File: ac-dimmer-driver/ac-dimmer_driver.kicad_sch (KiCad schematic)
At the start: 10 parts, among them J1 Conn_01x08_Pin, J2 Conn_01x08_Pin, U1 MCP4451

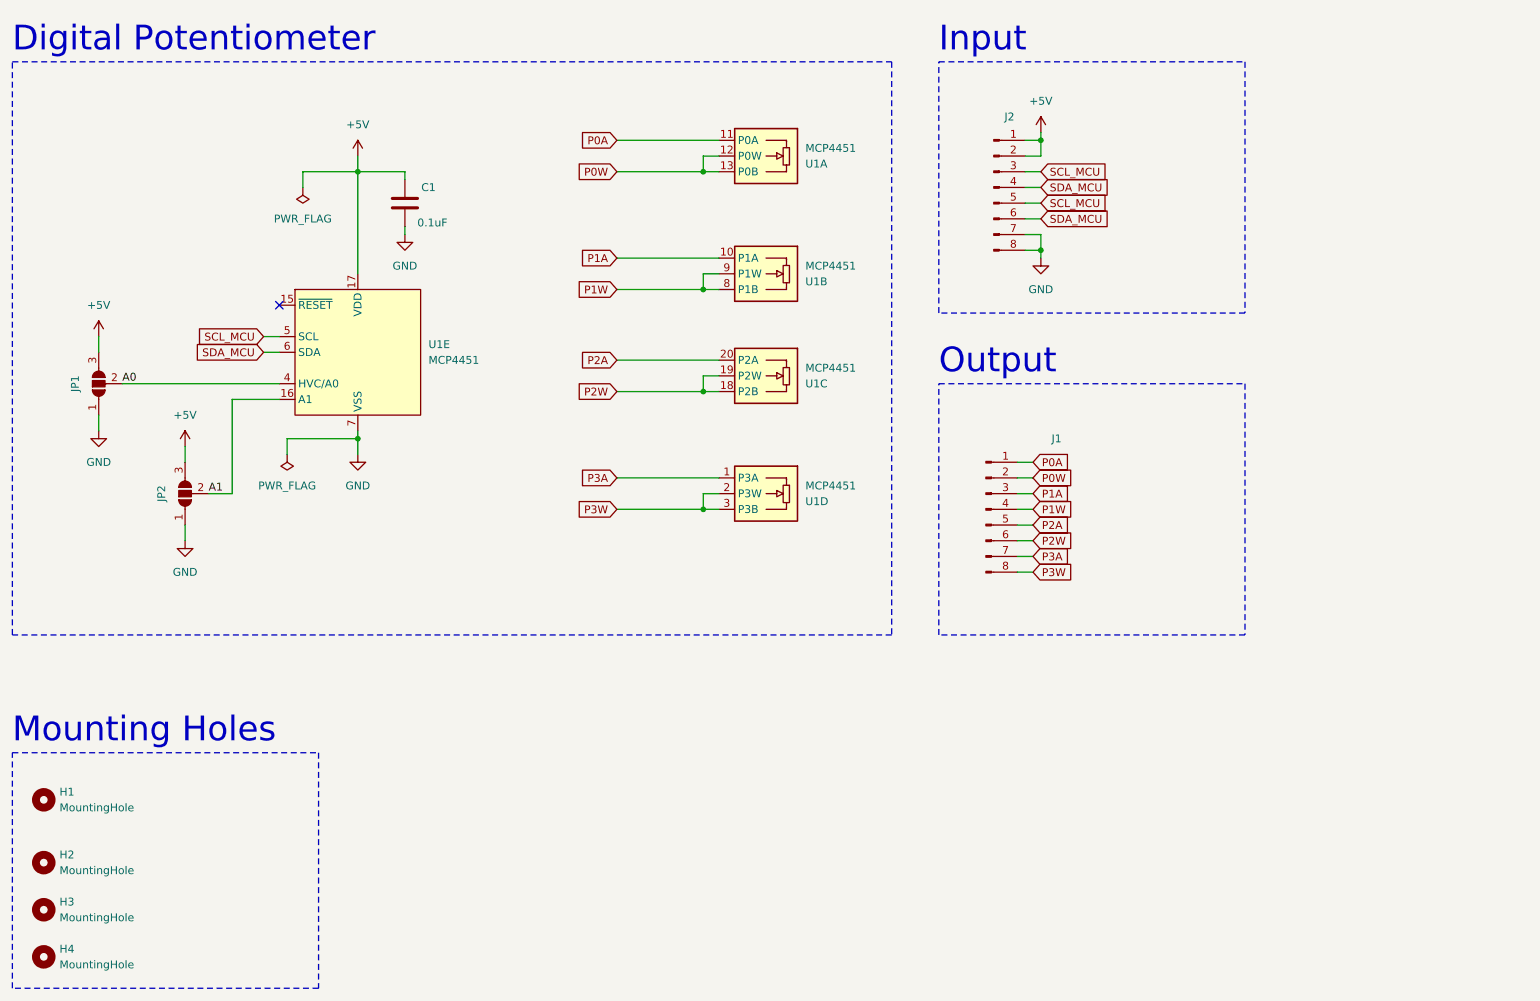
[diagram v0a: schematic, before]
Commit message: Create production files for ac dimmer
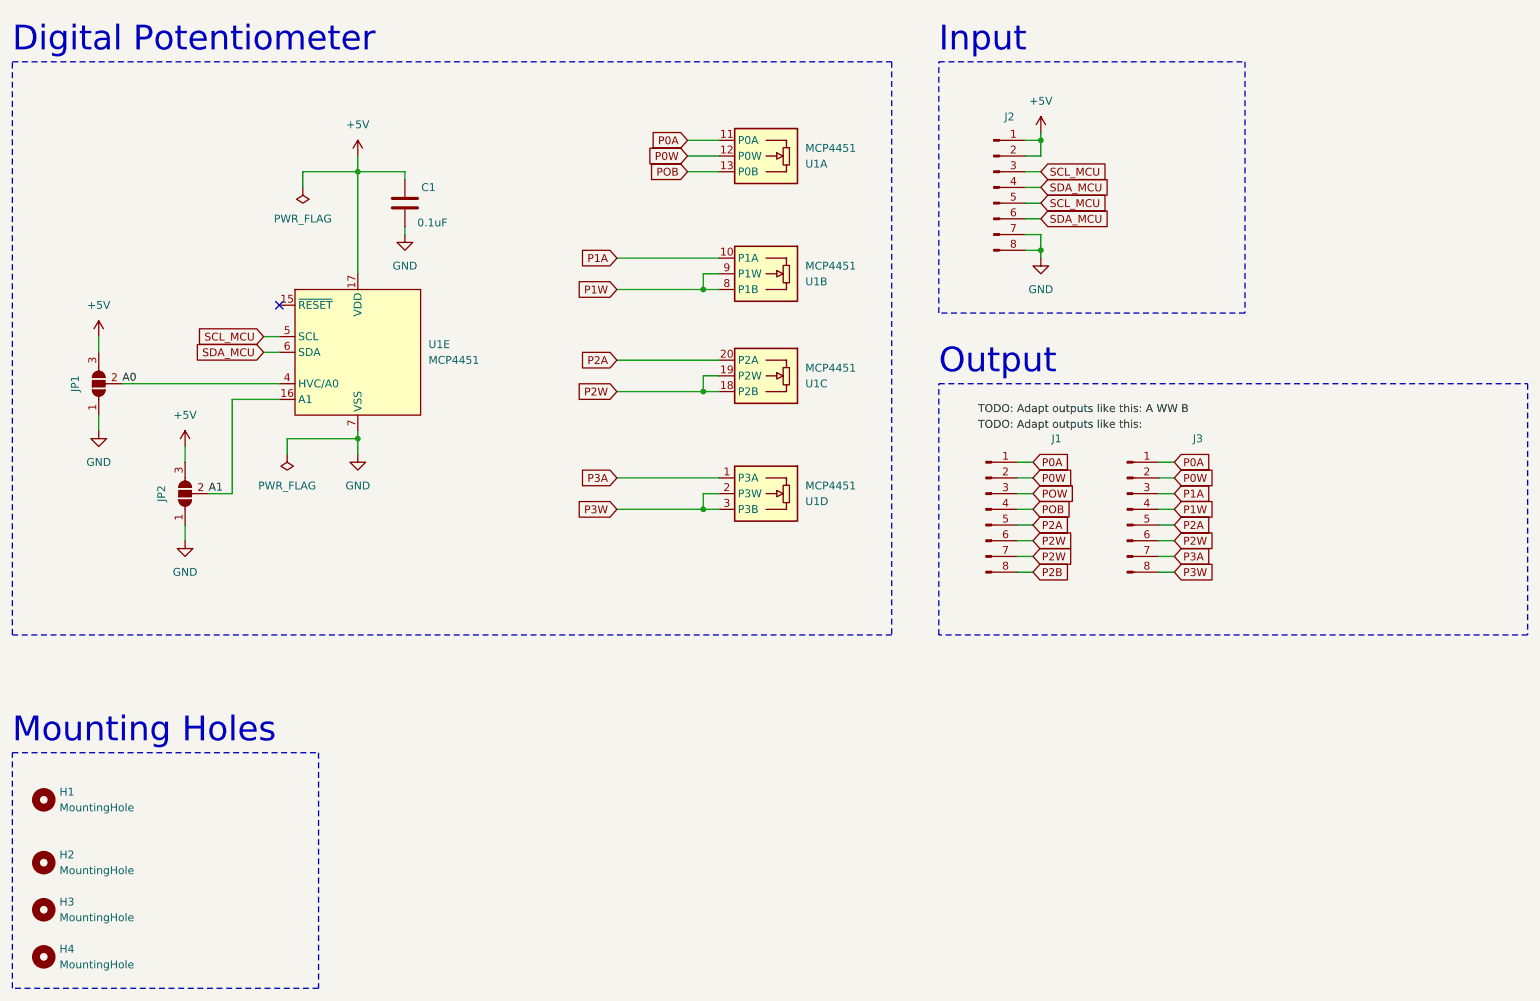
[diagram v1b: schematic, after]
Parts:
- added J3: Conn_01x08_Pin, Connector_PinHeader_2.54mm:PinHeader_1x08_P2.54mm_Vertical, symbol Connector:Conn_01x08_Pin
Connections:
- net P0A: now also J3.1 (Pin_1)
- net P0W: now also J3.2 (Pin_2); no longer U1.13 (P0B)
- net P1A: now also J3.3 (Pin_3); no longer J1.3 (Pin_3)
- net P1W: now also J3.4 (Pin_4); no longer J1.4 (Pin_4)
- net P2A: now also J3.5 (Pin_5)
- net P2W: now also J1.7 (Pin_7), J3.6 (Pin_6)
- net P3A: now also J3.7 (Pin_7); no longer J1.7 (Pin_7)
- net P3W: now also J3.8 (Pin_8); no longer J1.8 (Pin_8)
- new net P2B: J1.8 (Pin_8)
- new net POB: J1.4 (Pin_4), U1.13 (P0B)
- new net POW: J1.3 (Pin_3)
